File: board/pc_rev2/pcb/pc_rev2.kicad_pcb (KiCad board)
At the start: 4 copper layers, 200 x 100 mm, 104 parts, among them J1 GND Pins, J2 Conn_01x24, J3 Conn_01x24, J4 Conn_01x05, Q1 SSM3J332R, Q2 BSS138, Q3 BSS138, SW1 SW_Push, SW10 SW_Push, SW11 SW_Push, SW12 SW_Push, SW13 SW_Push, SW14 SW_Push, SW15 SW_Push, SW16 SW_Push, SW17 SW_Push, SW18 SW_Push, SW19 SW_Push, SW2 SW_Push, SW20 SW_Push, SW21 SW_Push, SW22 SW_Push, SW23 SW_Push, SW24 SW_Push, SW25 SW_Push, SW26 SW_Push, SW27 SW_Push, SW28 SW_Push, SW29 SW_Push, SW3 SW_Push, SW30 SW_Push, SW31 SW_Push, SW32 SW_Push, SW33 SW_Push, SW34 SW_Push, SW35 SW_Push, SW36 SW_Push, SW37 SW_Push, SW38 SW_Push, SW39 SW_Push, SW4 SW_Push, SW40 SW_Push, SW41 SW_Push, SW42 SW_Push, SW43 SW_Push, SW44 SW_Push, SW45 SW_Push, SW46 SW_Push, SW47 SW_Push, SW48 SW_Push, SW49 SW_Push, SW5 SW_Push, SW50 SW_Push, SW51 SW_Push, SW52 SW_Push, SW53 SW_Push, SW54 SW_Push, SW55 SW_Push, SW56 SW_Push, SW57 SW_Push, SW58 SW_Push, SW59 SW_Push, SW6 SW_Push, SW60 SW_Push, SW61 SW_Push, SW62 SW_Push, SW63 SW_Push, SW64 SW_Push, SW7 SW_Push, SW8 SW_Push, SW9 SW_Push, U1 AE-FT234X, U2 Tang_nano_9K, U3 SC2004CSWB-XA-LB-G, U4 NJM2742D, U5 4066, U6 TC75S103F, U7 NJU7109, U8 OLED

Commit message: 諸々改良＆基板デザイン（WIP）
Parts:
- removed H5: MountingHole, MountingHole:MountingHole_3.2mm_M3
- removed Q2, Q3: BSS138, Package_TO_SOT_SMD:SOT-23_Handsoldering
- removed SW1, SW10, SW11, SW12, SW13, SW14, SW15, SW16, SW17, SW18, SW19, SW2, SW20, SW21, SW22, SW23, SW24, SW25, SW26, SW27, SW28, SW29, SW3, SW30, SW31, SW32, SW33, SW34, SW35, SW36, SW37, SW38, SW39, SW4, SW40, SW41, SW42, SW43, SW44, SW45, SW46, SW47, SW48, SW49, SW5, SW50, SW51, SW52, SW53, SW54, SW55, SW56, SW57, SW58, SW59, SW6, SW60, SW61, SW62, SW63, SW64, SW7, SW8, SW9: SW_Push, Button_Switch_THT:SW_PUSH_6mm_H7.3mm
- removed U7: NJU7109, Package_TO_SOT_SMD:SOT-23-5
- added C1: 100nF, Capacitor_SMD:C_0603_1608Metric_Pad1.08x0.95mm_HandSolder, F.Cu at (109.6, 104.7)
- added C10: 100nF, Capacitor_SMD:C_0603_1608Metric_Pad1.08x0.95mm_HandSolder, F.Cu at (112.1, 50.5)
- added C11: 100pF, Capacitor_SMD:C_0603_1608Metric_Pad1.08x0.95mm_HandSolder, F.Cu at (113.4, 74.2)
- added C12: 100nF, Capacitor_SMD:C_0603_1608Metric_Pad1.08x0.95mm_HandSolder, F.Cu at (121.7, 67.2)
- added C13: 100nF, Capacitor_SMD:C_0603_1608Metric_Pad1.08x0.95mm_HandSolder, F.Cu at (117.9, 57.1)
- added C14: 100n, Capacitor_SMD:C_0603_1608Metric_Pad1.08x0.95mm_HandSolder, F.Cu at (66.4, 112.9)
- added C15: 100nF, Capacitor_SMD:C_0603_1608Metric_Pad1.08x0.95mm_HandSolder, F.Cu at (123.6, 53.2)
- added C16: 100nF, Capacitor_SMD:C_0603_1608Metric_Pad1.08x0.95mm_HandSolder, F.Cu at (132.5, 54.5)
- added C17: 100nF, Capacitor_SMD:C_0603_1608Metric_Pad1.08x0.95mm_HandSolder, F.Cu at (122.9, 125.6)
- added C9: 470uF, Capacitor_THT:CP_Radial_D8.0mm_P3.50mm, F.Cu at (129.0, 127.5)
- added D1: 1N4148, Diode_THT:D_DO-34_SOD68_P7.62mm_Horizontal, F.Cu at (64.5, 120.5)
- added D2: BAT54S, Package_TO_SOT_SMD:SOT-23, F.Cu at (132.5, 71.7)
- added J10: Conn_01x05, Connector_PinHeader_2.54mm:PinHeader_1x03_P2.54mm_Vertical, F.Cu at (123.6, 58.3)
- added J11: Conn_01x03, Connector_PinHeader_2.54mm:PinHeader_1x03_P2.54mm_Vertical, F.Cu at (140.7, 52.0)
- added J12: GND Pins, Connector_PinHeader_2.54mm:PinHeader_1x02_P2.54mm_Vertical, F.Cu at (100.1, 130.7)
- added J13: Conn_01x02, Connector_PinHeader_2.54mm:PinHeader_1x02_P2.54mm_Vertical, F.Cu at (131.2, 104.7)
- added J14: Conn_01x03, Connector_PinHeader_2.54mm:PinHeader_1x03_P2.54mm_Vertical, F.Cu at (140.7, 85.0)
- added J15: INPUT, Connector_JST:JST_XH_S3B-XH-A_1x03_P2.50mm_Horizontal, F.Cu at (51.8, 118.0)
- added J16: OUTPUT, Connector_JST:JST_XH_S3B-XH-A_1x03_P2.50mm_Horizontal, F.Cu at (51.8, 105.3)
- added J17: GND Pins, Connector_PinHeader_2.54mm:PinHeader_1x02_P2.54mm_Vertical, F.Cu at (138.2, 99.0)
- added J18: Conn_01x05, Connector_PinHeader_2.54mm:PinHeader_1x03_P2.54mm_Vertical, F.Cu at (100.1, 115.5)
- added J19: Conn_01x02, Connector_PinHeader_2.54mm:PinHeader_1x02_P2.54mm_Vertical, F.Cu at (131.2, 81.8)
- added J20: Conn_01x03, Connector_PinHeader_2.54mm:PinHeader_1x03_P2.54mm_Vertical, F.Cu at (124.8, 83.7)
- added J21: Conn_Grove_Host, uchan:Grove_1x04_P2mm_THT_Horizontal, F.Cu at (72.1, 128.8)
- added J5: Conn_Grove_Host, uchan:Grove_1x04_P2mm_THT_Horizontal, F.Cu at (107.7, 41.1)
- added J6: Conn_01x03, Connector_JST:JST_XH_S2B-XH-A_1x02_P2.50mm_Horizontal, F.Cu at (138.2, 107.8)
- added J7: Conn_01x03, Connector_JST:JST_XH_S2B-XH-A_1x02_P2.50mm_Horizontal, F.Cu at (138.2, 120.5)
- added J8: Conn_Grove-Analog_Host, uchan:Grove_1x04_P2mm_THT_Horizontal, F.Cu at (138.2, 62.1)
- added J9: Conn_Grove-Analog_Host, uchan:Grove_1x04_P2mm_THT_Horizontal, F.Cu at (138.2, 73.9)
- added R10: 100k, Resistor_SMD:R_0603_1608Metric_Pad0.98x0.95mm_HandSolder, F.Cu at (118.5, 86.9)
- added R11: 100k, Resistor_SMD:R_0603_1608Metric_Pad0.98x0.95mm_HandSolder, F.Cu at (114.0, 90.1)
- added R12: 33, Resistor_SMD:R_0603_1608Metric_Pad0.98x0.95mm_HandSolder, F.Cu at (117.9, 116.1)
- added R13: 33, Resistor_SMD:R_0603_1608Metric_Pad0.98x0.95mm_HandSolder, F.Cu at (115.3, 116.1)
- added R14: 10k, Resistor_SMD:R_0603_1608Metric_Pad0.98x0.95mm_HandSolder, F.Cu at (119.8, 121.8)
- added R15: 10k, Resistor_SMD:R_0603_1608Metric_Pad0.98x0.95mm_HandSolder, F.Cu at (133.7, 119.3)
- added R17: 22k, Resistor_SMD:R_0603_1608Metric_Pad0.98x0.95mm_HandSolder, F.Cu at (100.1, 62.8)
- added R18: 11k, Resistor_SMD:R_0603_1608Metric_Pad0.98x0.95mm_HandSolder, F.Cu at (105.2, 63.4)
- added R19: 22k, Resistor_SMD:R_0603_1608Metric_Pad0.98x0.95mm_HandSolder, F.Cu at (100.1, 67.2)
- added R20: 11k, Resistor_SMD:R_0603_1608Metric_Pad0.98x0.95mm_HandSolder, F.Cu at (105.2, 67.9)
- added R21: 22k, Resistor_SMD:R_0603_1608Metric_Pad0.98x0.95mm_HandSolder, F.Cu at (100.1, 71.7)
- added R22: 11k, Resistor_SMD:R_0603_1608Metric_Pad0.98x0.95mm_HandSolder, F.Cu at (105.2, 72.3)
- added R23: 22k, Resistor_SMD:R_0603_1608Metric_Pad0.98x0.95mm_HandSolder, F.Cu at (100.1, 76.1)
- added R24: 11k, Resistor_SMD:R_0603_1608Metric_Pad0.98x0.95mm_HandSolder, F.Cu at (105.2, 76.7)
- added R25: 22k, Resistor_SMD:R_0603_1608Metric_Pad0.98x0.95mm_HandSolder, F.Cu at (100.1, 79.9)
- added R26: 11k, Resistor_SMD:R_0603_1608Metric_Pad0.98x0.95mm_HandSolder, F.Cu at (105.2, 81.2)
- added R27: 22k, Resistor_SMD:R_0603_1608Metric_Pad0.98x0.95mm_HandSolder, F.Cu at (100.1, 84.4)
- added R28: 11k, Resistor_SMD:R_0603_1608Metric_Pad0.98x0.95mm_HandSolder, F.Cu at (105.2, 85.6)
- added R29: 22k, Resistor_SMD:R_0603_1608Metric_Pad0.98x0.95mm_HandSolder, F.Cu at (100.1, 88.8)
- added R30: 11k, Resistor_SMD:R_0603_1608Metric_Pad0.98x0.95mm_HandSolder, F.Cu at (105.2, 90.1)
- added R31: 22k, Resistor_SMD:R_0603_1608Metric_Pad0.98x0.95mm_HandSolder, F.Cu at (100.1, 93.3)
- added R32: 22k, Resistor_SMD:R_0603_1608Metric_Pad0.98x0.95mm_HandSolder, F.Cu at (105.2, 94.5)
- added R33: 390, uchan:R_Axial_CF25_CFS50_L6.3mm_D2.3mm_P7.62mm_Horizontal, F.Cu at (56.9, 118.0)
- added R34: 33, uchan:R_Axial_CF25_CFS50_L6.3mm_D2.3mm_P7.62mm_Horizontal, F.Cu at (64.5, 105.3)
- added R35: 10, uchan:R_Axial_CF25_CFS50_L6.3mm_D2.3mm_P7.62mm_Horizontal, F.Cu at (64.5, 107.8)
- added R36: 4.7k, Resistor_SMD:R_0603_1608Metric_Pad0.98x0.95mm_HandSolder, F.Cu at (69.0, 109.8)
- added R37: 100k, Resistor_SMD:R_0603_1608Metric_Pad0.98x0.95mm_HandSolder, F.Cu at (118.5, 93.3)
- added R38: 10k, Resistor_SMD:R_0603_1608Metric_Pad0.98x0.95mm_HandSolder, F.Cu at (128.7, 75.5)
- added U10: MCP1501-30xCH, Package_TO_SOT_SMD:SOT-23-6, F.Cu at (127.4, 53.2)
- added U9: TLP2361, Package_SO:SO-5-6_4.55x3.7mm_P1.27mm, F.Cu at (60.1, 112.9)
- C2: value 1.5nF -> 100nF; footprint Capacitor_THT:C_Disc_D4.3mm_W1.9mm_P5.00mm -> Capacitor_SMD:C_0603_1608Metric_Pad1.08x0.95mm_HandSolder
- C3: value 680pF -> 100nF; footprint Capacitor_THT:C_Disc_D4.3mm_W1.9mm_P5.00mm -> Capacitor_SMD:C_0603_1608Metric_Pad1.08x0.95mm_HandSolder
- C4: value 100pF -> 2000pF; footprint Capacitor_THT:C_Disc_D4.3mm_W1.9mm_P5.00mm -> Capacitor_SMD:C_0603_1608Metric_Pad1.08x0.95mm_HandSolder
- C5: value 100nF -> 10uF
- C6: value 100nF -> 1uF
- J1: value GND Pins -> Conn_02x13_Odd_Even; footprint Connector_PinHeader_2.54mm:PinHeader_1x04_P2.54mm_Vertical -> Connector_PinHeader_2.54mm:PinHeader_2x14_P2.54mm_Vertical
- J2: value Conn_01x24 -> Conn_02x08_Row_Letter_Last; footprint Connector_PinHeader_2.54mm:PinHeader_1x24_P2.54mm_Vertical -> Connector_PinHeader_2.54mm:PinHeader_2x08_P2.54mm_Vertical
- J3: value Conn_01x24 -> Conn_02x06_Row_Letter_Last; footprint Connector_PinHeader_2.54mm:PinHeader_1x24_P2.54mm_Vertical -> Connector_PinHeader_2.54mm:PinHeader_2x06_P2.54mm_Vertical
- J4: value Conn_01x05 -> Conn_02x10_Row_Letter_Last; footprint Connector_PinHeader_2.54mm:PinHeader_1x05_P2.54mm_Vertical -> Connector_PinHeader_2.54mm:PinHeader_2x10_P2.54mm_Vertical
- LS1: value PKM13EPYH4000-A0 -> 13mm
- Q1: value SSM3J332R -> BC817BPN; footprint Package_TO_SOT_SMD:SOT-23_Handsoldering -> Package_TO_SOT_SMD:SOT-457T
- R1: value 47 -> 0.5M; footprint Resistor_THT:R_Axial_DIN0207_L6.3mm_D2.5mm_P7.62mm_Horizontal -> OptoDevice:R_LDR_D6.4mm_P3.4mm_Vertical
- R2: value 0.5M -> 2.2k; footprint OptoDevice:R_LDR_D6.4mm_P3.4mm_Vertical -> Resistor_SMD:R_0603_1608Metric_Pad0.98x0.95mm_HandSolder
- R3: value 16k -> 100k
- R4, R5: value 4.7k -> 100k
- R6: value 16k -> 20k
- R7: value 2k -> 200
- R8: value 100 -> 2.2k
- R9: value 2k -> 100k
- RV1: footprint Potentiometer_THT:Potentiometer_Vishay_T73XX_Horizontal -> uchan:Potentiometer_Suntan_TSR-3386K_Vertical
- RV2: footprint uchan:Potentiometer_Suntan_TSR-065_Vertical -> uchan:Potentiometer_Suntan_TSR-3386K_Vertical
- RV3: value 5k -> 50k; footprint Potentiometer_THT:Potentiometer_Vishay_T73XX_Horizontal -> uchan:Potentiometer_Suntan_TSR-3386K_Vertical
- U1: value AE-FT234X -> Tang_nano_9K; footprint uchan:AE-FT234X -> uchan:DIP-48_Tang-Nano-9K
- U2: value Tang_nano_9K -> SKU2782; footprint uchan:DIP-48_Tang-Nano-9K -> uchan:SKU2782
- U3: value SC2004CSWB-XA-LB-G -> LMV324B; footprint uchan:SC2004C_float -> Package_SO:TSSOP-14_4.4x5mm_P0.65mm
- U4: value NJM2742D -> LMV324B; footprint Package_DIP:DIP-8_W7.62mm -> Package_SO:TSSOP-14_4.4x5mm_P0.65mm
- U5: value 4066 -> TC74HC4066AF; footprint Package_DIP:DIP-14_W7.62mm -> Package_SO:SO-14_5.3x10.2mm_P1.27mm
- U6: value TC75S103F -> TPCMP231; footprint Package_TO_SOT_SMD:TSOT-23-5 -> Package_TO_SOT_SMD:SOT-23-5
- U8: value OLED -> 74HC4051; footprint uchan:OLED_Display_I2C -> Package_SO:SOIC-16W_5.3x10.2mm_P1.27mm
- moved H2 210.2 mm to (50.0, 130.0)
- moved J2 192.1 mm to (49.3, 49.4), turned to 0 degrees
- moved J3 156.4 mm to (89.9, 39.3), turned to 0 degrees
- moved U2 141.7 mm to (100.1, 39.3), turned to 0 degrees
- moved J1 136.3 mm to (92.5, 90.1), turned to 180 degrees
- moved H4 134.5 mm to (140.0, 40.0)
- moved R4 116.2 mm to (112.1, 104.7), turned to 90 degrees
- moved R5 107.8 mm to (119.5, 100.9)
- moved U8 93.9 mm to (130.6, 62.1)
- moved H3 90.0 mm to (140.0, 130.0)
- moved RV3 85.2 mm to (126.6, 115.7)
- moved U1 80.7 mm to (82.3, 97.7), turned to 180 degrees
- moved U3 78.7 mm to (120.4, 107.2)
- moved RV1 73.5 mm to (84.8, 111.7), turned to -90 degrees
- moved Q1 73.0 mm to (122.9, 128.8), turned to 0 degrees
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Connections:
- C2 pad 1: Net-(C2-Pad1) -> /audio/mic_in
- C2 pad 2: /ADC/dac_out -> /audio/mic_opin
- C3 pad 2: Net-(U4B-+) -> +5V
- C4 pad 1: Net-(C4-Pad1) -> Net-(U3D--)
- C4 pad 2: GND -> /audio/mic_mid
- C5 pad 1: +5V -> Net-(C5-Pad1)
- C6 pad 1: GND -> Net-(C6-Pad1)
- C6 pad 2: +5V -> GND
- C7 pad 1: +5V -> Net-(C7-Pad1)
- C8 pad 1: +5V -> Net-(C8-Pad1)
- C8 pad 2: GND -> /audio/spk_opin
- J1 pad 2: GND -> /ADC/vref_d0
- J1 pad 4: GND -> /ADC/vref_d1
- J2 pad 1: Net-(J2-Pin_1) -> GND
- J2 pad 10: /ROW6 -> /mcu/gpio4
- J2 pad 11: /ROW7 -> GND
- J2 pad 12: /ROW8 -> /mcu/gpio5
- J2 pad 13: /SCL -> GND
- J2 pad 14: /SDA -> /beep
- J2 pad 15: Net-(J2-Pin_15) -> GND
- J2 pad 16: Net-(J2-Pin_16) -> /mcu/gpio7
- J2 pad 2: Net-(J2-Pin_2) -> /mcu/gpio0
- J2 pad 3: Net-(J2-Pin_3) -> GND
- J2 pad 4: Net-(J2-Pin_4) -> /mcu/gpio1
- J2 pad 5: /ROW1 -> GND
- J2 pad 6: /ROW2 -> /mcu/gpio2
- J2 pad 7: /ROW3 -> GND
- J2 pad 8: /ROW4 -> /mcu/gpio3
- J2 pad 9: /ROW5 -> GND
- J3 pad 1: /RS -> /uart_rx
- J3 pad 10: /RW -> GND
- J3 pad 11: /E -> /sericon_tx
- J3 pad 12: Net-(J3-Pin_12) -> GND
- J3 pad 2: /COL8 -> GND
- J3 pad 3: /COL7 -> /uart_tx
- J3 pad 4: /COL6 -> GND
- J3 pad 5: /COL5 -> /msmp_rx
- J3 pad 6: /COL4 -> GND
- J3 pad 7: /COL3 -> /msmp_tx
- J3 pad 8: /COL2 -> GND
- J3 pad 9: /COL1 -> /sericon_rx
- J4 pad 1: /ADC/sh_buf -> GND
- J4 pad 2: /ADC/ain_buf -> /mcu/dbgio0
- J4 pad 3: /ADC/sh_on_5v -> GND
- J4 pad 4: /ADC/dac_out -> /mcu/dbgio1
- Q1 pad 1: Net-(J3-Pin_12) -> /audio/spk_opout
- Q1 pad 2: +5V -> Net-(Q1A-B1)
- Q1 pad 3: Net-(Q1-D) -> GND
- R1 pad 1: Net-(Q1-D) -> +3.3V
- R1 pad 2: Net-(U3-A) -> /ADC/ain1
- R2 pad 1: +5V -> +3.3V
- R2 pad 2: /ADC/ain -> /audio/mic_in
- R3 pad 1: /adc_dac_pwm -> +3.3V
- R3 pad 2: Net-(C2-Pad1) -> Net-(U3A-+)
- R4 pad 1: /SCL -> Net-(U3A-+)
- R4 pad 2: +3.3V -> GND
- R5 pad 1: /SDA -> /audio/mic_opin
- R5 pad 2: +3.3V -> GNDREF
- R6 pad 1: Net-(C2-Pad1) -> Net-(U3D--)
- R6 pad 2: Net-(U4B-+) -> /audio/mic_mid
- R7 pad 1: +5V -> Net-(U3D--)
- R7 pad 2: /ADC/sh_on_5v -> Net-(C5-Pad1)
- R8 pad 1: Net-(U6-+) -> Net-(U3C--)
- R8 pad 2: Net-(C4-Pad1) -> Net-(C6-Pad1)
- R9 pad 1: +3.3V -> +5V
- R9 pad 2: /adc_cmp -> Net-(C7-Pad1)
- RV1 pad 1: +3.3V -> /beep
- RV1 pad 2: Net-(U3-VO) -> Net-(LS1-Pad1)
- RV2 pad 1: /ADC/ain -> /ADC/ain1
- RV3 pad 1: Net-(J3-Pin_13) -> Net-(U3C--)
- RV3 pad 2: Net-(LS1-Pad1) -> Net-(U3C--)
- RV3 pad 3: GND -> Net-(R38-Pad1)
- U1 pad 1: unconnected-(U1-5V-Pad1) -> /mcu/tf_cs
- U1 pad 2: GND -> /mcu/tf_mosi
- U1 pad 3: /RX -> /mcu/tf_sclk
- U1 pad 4: /TX -> /mcu/tf_miso
- U1 pad 5: unconnected-(U1-CB0-Pad5) -> /ADC/vref_d0
- U2 pad 1: Net-(J2-Pin_1) -> unconnected-(U2-DTR-Pad1)
- U2 pad 2: Net-(J2-Pin_2) -> /uart_tx
- U2 pad 3: Net-(J2-Pin_3) -> /uart_rx
- U2 pad 4: Net-(J2-Pin_4) -> unconnected-(U2-VCC-Pad4)
- U2 pad 5: /ROW1 -> unconnected-(U2-CTS-Pad5)
- U2 pad 6: /ROW2 -> GND
- U3 pad 1: GND -> GNDREF
- U3 pad 10: unconnected-(U3-DB3-Pad10) -> /audio/mic_mid
- U3 pad 11: /DB4 -> GND
- U3 pad 12: /DB5 -> /audio/mic_opin
- U3 pad 13: /DB6 -> Net-(U3D--)
- U3 pad 14: /DB7 -> /audio/mic_mid
- U3 pad 2: +3.3V -> GNDREF
- U3 pad 3: Net-(U3-VO) -> Net-(U3A-+)
- U3 pad 4: /RS -> +5V
- U3 pad 5: /RW -> /audio/spk_opin
- U3 pad 6: /E -> Net-(U3B--)
- U3 pad 7: unconnected-(U3-DB0-Pad7) -> /audio/spk_mid
- U3 pad 8: unconnected-(U3-DB1-Pad8) -> Net-(R38-Pad1)
- U3 pad 9: unconnected-(U3-DB2-Pad9) -> Net-(U3C--)
- U4 pad 1: /ADC/ain_buf -> /ADC/sh_buf
- U4 pad 2: /ADC/ain_buf -> /ADC/sh_buf
- U4 pad 3: /ADC/ain -> Net-(U4A-+)
- U4 pad 4: GND -> +5V
- U4 pad 5: Net-(U4B-+) -> GND
- U4 pad 6: /ADC/dac_out -> Net-(U4B--)
- U4 pad 7: /ADC/dac_out -> Net-(U4B--)
- U4 pad 8: +5V -> /ADC/ain_buf
- U5 pad 1: /ADC/ain_buf -> /ADC/dac_out
- U5 pad 10: unconnected-(U5-Pad10) -> GND
- U5 pad 11: unconnected-(U5-Pad11) -> GND
- U5 pad 13: /ADC/sh_on_5v -> /audio/spk_on
- U5 pad 14: +5V -> +3.3V
- U5 pad 2: Net-(U6-+) -> Net-(C8-Pad1)
- U5 pad 3: unconnected-(U5-Pad3) -> /ADC/ain_buf
- U5 pad 4: unconnected-(U5-Pad4) -> Net-(U4A-+)
- U5 pad 5: GND -> /ADC/sh_on
- U5 pad 8: unconnected-(U5-Pad8) -> GND
- U5 pad 9: unconnected-(U5-Pad9) -> GND
- U6 pad 1: /ADC/sh_buf -> /ADC/cmp
- U6 pad 3: Net-(U6-+) -> /ADC/sh_buf
- U6 pad 4: /ADC/sh_buf -> /ADC/dac_raw
- U6 pad 5: +5V -> +3.3V
- U8 pad 1: GND -> /ADC/ain4
- U8 pad 2: +3.3V -> /ADC/dac_out
- U8 pad 3: /SCL -> Net-(U4C-+)
- U8 pad 4: /SDA -> Net-(U10-OUT)
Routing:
- net /COL6: track 330.2 -> 0.00 mm, vias 2 -> 0
- net /COL1: track 294.0 -> 0.00 mm, vias 2 -> 0
- net /COL7: track 293.3 -> 0.00 mm, vias 1 -> 0
- net /COL2: track 293.2 -> 0.00 mm, vias 2 -> 0
- net /COL3: track 275.4 -> 0.00 mm, vias 2 -> 0
- net /COL4: track 274.7 -> 0.00 mm, vias 2 -> 0
- net /COL5: track 267.7 -> 0.00 mm, vias 2 -> 0
- net /ROW6: track 266.0 -> 0.00 mm, vias 1 -> 0
- net /ROW7: track 240.1 -> 0.00 mm, vias 1 -> 0
- net /ROW2: track 236.8 -> 0.00 mm, vias 2 -> 0
- net /COL8: track 229.6 -> 0.00 mm
- net /ROW1: track 226.0 -> 0.00 mm, vias 1 -> 0
- net /ROW5: track 218.9 -> 0.00 mm, vias 1 -> 0
- net /ROW3: track 215.7 -> 0.00 mm, vias 1 -> 0
- net /RS: track 199.8 -> 0.00 mm
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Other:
- board size 200 x 100 mm -> 100 x 100 mm
- copper layers 4 -> 2
- board text added: "1.65V"
- board text added: "10k"
- board text added: "2.5V"
- board text added: "33"
- board text added: "470uF"
- board text added: "50k"
- board text removed: ", <"
- board text removed: "- ="
- board text removed: ". >"
- board text removed: "/ ?"
- board text removed: "0"
- board text removed: "1 !"
- board text removed: "2 {dblquote}"
- board text removed: "2024/09/27 Rev.1 Kota Uchida Cybozu Labs, Inc."
- board text removed: "3 #"
- board text removed: "3.3V"
- board text removed: "4 $"
- board text removed: "5 %"
- board text removed: "5V"
- board text removed: "6 &"
- board text removed: "7 '"
- board text removed: "8 ("
- board text removed: "9 )"
- board text removed: ": *"
- board text removed: "; +"
- board text removed: "@ `"
- board text removed: "A"
- board text removed: "Alt"
- board text removed: "B"
- board text removed: "BL"
- board text removed: "BS"
- board text removed: "C"
- board text removed: "COL1"
- board text removed: "COL2"
- board text removed: "COL5"
- board text removed: "COL6"
- board text removed: "COL7"
- board text removed: "COL8"
- board text removed: "CS"
- board text removed: "Caps"
- board text removed: "ComProc PC"
- board text removed: "Contrast"
- board text removed: "Ctrl"
- board text removed: "D"
- board text removed: "DB4"
- board text removed: "DB5"
- board text removed: "DB6"
- board text removed: "DB7"
- board text removed: "E"
- board text removed: "E/J"
- board text removed: "Enter"
- board text removed: "F"
- board text removed: "G"
- board text removed: "GND"
- board text removed: "H"
- board text removed: "I"
- board text removed: "J"
- board text removed: "JLCJLCJLCJLC"
- board text removed: "K"
- board text removed: "Kana"
- board text removed: "L"
- board text removed: "M"
- board text removed: "MO"
- board text removed: "N"
- board text removed: "O"
- board text removed: "P"
- board text removed: "P41"
- board text removed: "P42"
- board text removed: "P51"
- board text removed: "P68"
- board text removed: "P69"
- board text removed: "P70"
- board text removed: "P71"
- board text removed: "P72"
- board text removed: "P73"
- board text removed: "P74"
- board text removed: "Q"
- board text removed: "R"
- board text removed: "ROW1"
- board text removed: "ROW2"
- board text removed: "ROW3"
- board text removed: "ROW4"
- board text removed: "ROW5"
- board text removed: "ROW6"
- board text removed: "ROW7"
- board text removed: "ROW8"
- board text removed: "RS"
- board text removed: "RW"
- board text removed: "RX"
- board text removed: "S"
- board text removed: "SCL"
- board text removed: "SDA"
- board text removed: "Shift"
- board text removed: "Space"
- board text removed: "T"
- board text removed: "TF_MISO"
- board text removed: "TF_SCLK"
- board text removed: "TX"
- board text removed: "Tab"
- board text removed: "U"
- board text removed: "V"
- board text removed: "Volume"
- board text removed: "W"
- board text removed: "X"
- board text removed: "Y"
- board text removed: "Z"
- board text removed: "[ {"
- board text removed: "\ _"
- board text removed: "] }"
- board text removed: "^ ~"
- board text removed: "ain"
- board text removed: "cmp"
- board text removed: "dac"
- board text removed: "dac_pwm"
- board text removed: "sh"
- board text removed: "sh_ctl"
- board text removed: "shon"
- board text removed: "←"
- board text removed: "↑"
- board text removed: "→"
- board text removed: "↓"
- board text removed: "変換"
- board text removed: "無変換"
- board text removed: "￥ |"

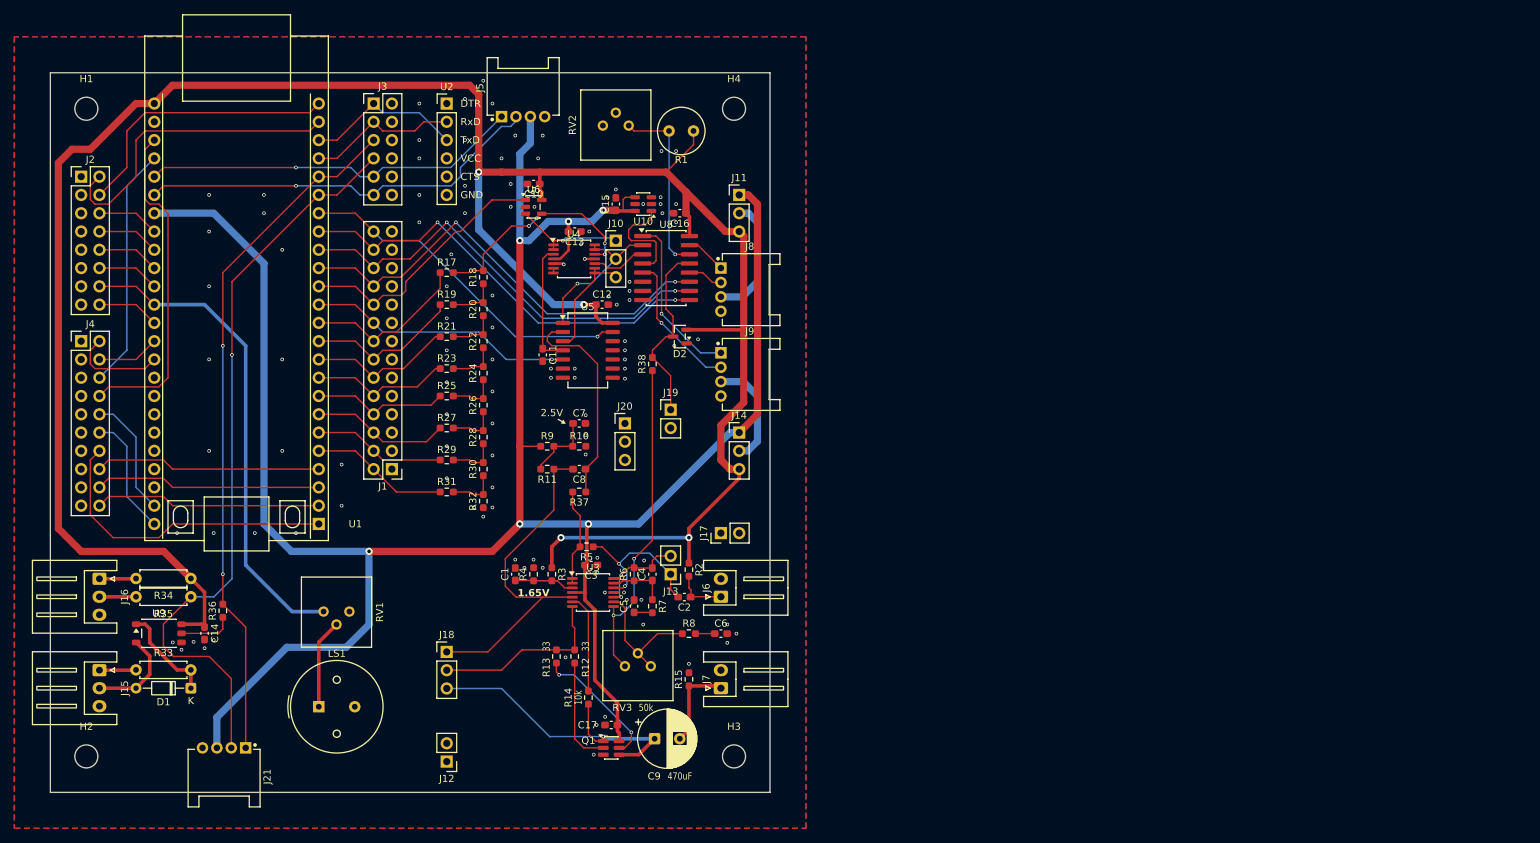
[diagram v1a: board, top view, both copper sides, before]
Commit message: Rev.2基板のシルク印刷を整える
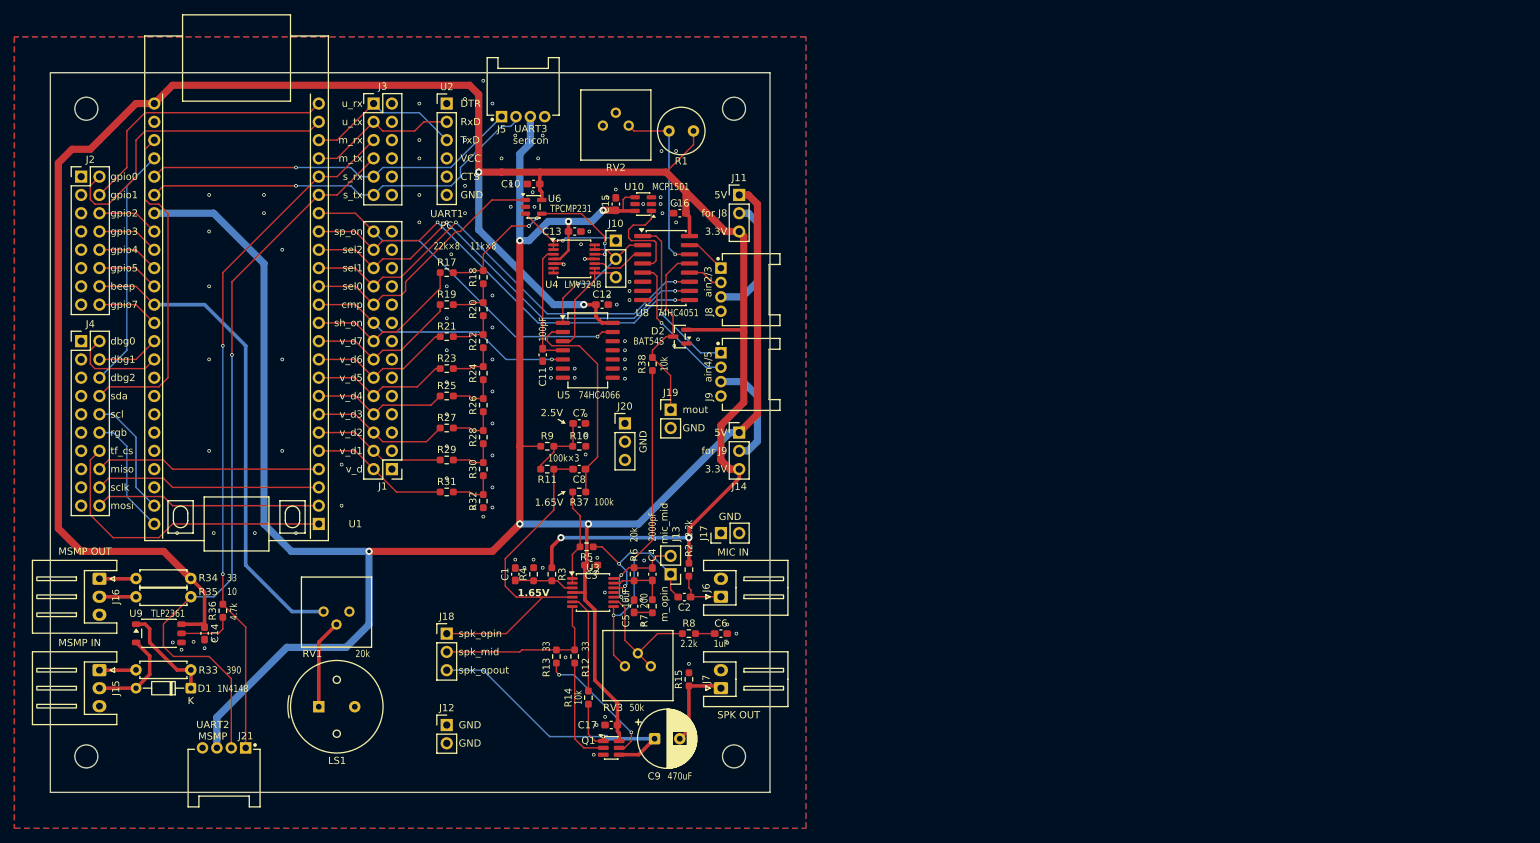
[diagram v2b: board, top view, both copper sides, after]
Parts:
- moved J12 5.08 mm to (100.1, 125.6), turned to 0 degrees
- moved J18 2.54 mm to (100.1, 112.9)
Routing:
- net /audio/spk_opout: track 44.9 -> 45.9 mm
- net /audio/spk_opin: track 48.2 -> 47.1 mm
- net /audio/spk_mid: track 25.1 -> 24.1 mm
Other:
- board text added: "10"
- board text added: "100k"
- board text added: "100k×3"
- board text added: "100pF"
- board text added: "10uF"
- board text added: "11k×8"
- board text added: "1N4148"
- board text added: "1uF"
- board text added: "2.2k"
- board text added: "200"
- board text added: "2000pF"
- board text added: "20k"
- board text added: "22k×8"
- board text added: "3.3V"
- board text added: "390"
- board text added: "4.7k"
- board text added: "5V"
- board text added: "74HC4051"
- board text added: "74HC4066"
- board text added: "BAT54S"
- board text added: "GND"
- board text added: "LMV324B"
- board text added: "MCP1501"
- board text added: "MIC IN"
- board text added: "MSMP IN"
- board text added: "MSMP OUT"
- board text added: "SPK OUT"
- board text added: "TLP2361"
- board text added: "TPCMP231"
- board text added: "UART1 PC"
- board text added: "UART2 MSMP"
- board text added: "UART3 sericon"
- board text added: "ain2/3"
- board text added: "ain4/5"
- board text added: "beep"
- board text added: "cmp"
- board text added: "dbg0"
- board text added: "dbg1"
- board text added: "dbg2"
- board text added: "for J8"
- board text added: "for J9"
- board text added: "gpio0"
- board text added: "gpio1"
- board text added: "gpio2"
- board text added: "gpio3"
- board text added: "gpio4"
- board text added: "gpio5"
- board text added: "gpio7"
- board text added: "m_opin"
- board text added: "m_rx"
- board text added: "m_tx"
- board text added: "mic_mid"
- board text added: "miso"
- board text added: "mosi"
- board text added: "mout"
- board text added: "rgb"
- board text added: "s_rx"
- board text added: "s_tx"
- board text added: "scl"
- board text added: "sclk"
- board text added: "sda"
- board text added: "sel0"
- board text added: "sel1"
- board text added: "sel2"
- board text added: "sh_on"
- board text added: "sp_on"
- board text added: "spk_mid"
- board text added: "spk_opin"
- board text added: "spk_opout"
- board text added: "tf_cs"
- board text added: "u_rx"
- board text added: "u_tx"
- board text added: "v_d"
- board text added: "v_d1"
- board text added: "v_d2"
- board text added: "v_d3"
- board text added: "v_d4"
- board text added: "v_d5"
- board text added: "v_d6"
- board text added: "v_d7"

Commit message: ポップノイズ防止用コンデンサ追加＆シルク微修正
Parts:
- added C18: 10nF, Capacitor_SMD:C_0603_1608Metric_Pad1.08x0.95mm_HandSolder, F.Cu at (122.9, 93.2)
- moved J18 2.54 mm to (100.1, 115.5)
- moved LS1 2.54 mm to (79.8, 123.1)
- moved RV1 2.46 mm to (82.3, 111.7)
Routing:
- net +5V: track 327.5 -> 324.4 mm
- net Net-(C18-Pad1): track 29.9 -> 32.5 mm
- net /beep: track 67.7 -> 65.3 mm
- net /audio/spk_opout: track 45.9 -> 44.9 mm
- net /audio/spk_opin: track 47.1 -> 48.2 mm
- net /audio/spk_mid: track 24.1 -> 25.1 mm
- net GND: vias 111 -> 114
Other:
- board text added: "01"
- board text added: "100k×2"
- board text added: "10nF"
- board text added: "2026/08/26 Rev.2 Kota Uchida Cybozu Labs, Inc."
- board text added: "8bit R-2R DAC"
- board text added: "BuntanPC"
- board text added: "CMP"
- board text added: "Hold Value"
- board text added: "Input"
- board text added: "Ref Vol"
- board text added: "SIG"
- board text added: "Sample & Hold"
- board text added: "Select"
- board text added: "mic_out"
- board text added: "opin"
- board text removed: "m_opin"
- board text removed: "mout"

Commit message: I2C用Groveコネクタを追加
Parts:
- added J22: Conn_Grove_I2C, uchan:Grove_1x04_P2mm_THT_Horizontal, F.Cu at (84.2, 128.8)
- added J23: Conn_01x03, Connector_PinHeader_2.54mm:PinHeader_1x03_P2.54mm_Vertical, F.Cu at (89.9, 125.6)
- moved LS1 15.3 mm to (78.6, 107.9)
- moved RV1 10.2 mm to (81.0, 121.8)
- moved J8 0.63 mm to (138.8, 62.1)
- moved J9 0.63 mm to (138.8, 73.9)
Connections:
- net /mcu/sda renamed /sda
- J4 pad 10: /mcu/scl -> /scl
- R1 pad 2: /ADC/ain1 -> /ADC/ain0
- RV2 pad 1: /ADC/ain1 -> /ADC/ain0
- U1 pad 47: /mcu/scl -> /mcu/rgbled
- U1 pad 48: /mcu/rgbled -> /scl
- U8 pad 13: /audio/mic_out -> /ADC/ain0
- U8 pad 14: /ADC/ain1 -> /audio/mic_out
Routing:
- net /scl: track 0.00 -> 66.9 mm
- net /sda: track 46.2 -> 105.5 mm, vias 0 -> 2
- net +3.3V: track 330.0 -> 386.6 mm
- net /ADC/ain0: track 0.00 -> 26.7 mm, vias 0 -> 1
- net /ADC/ain1: track 25.4 -> 0.00 mm, vias 1 -> 0
- net /mcu/scl: track 17.0 -> 0.00 mm
- net +5V: track 324.4 -> 338.0 mm
- net Net-(J22-VCC): track 0.00 -> 13.1 mm
- net /beep: track 65.3 -> 73.8 mm, vias 0 -> 1
- net Net-(LS1-Pad1): track 12.5 -> 15.0 mm
- net /mcu/tf_cs: track 43.3 -> 41.3 mm
- net /audio/mic_out: track 25.8 -> 27.3 mm
- net /mcu/rgbled: track 17.0 -> 15.5 mm
- net Net-(J14-Pin_2): track 15.3 -> 14.6 mm
- net Net-(J11-Pin_2): track 17.3 -> 16.6 mm
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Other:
- board text added: "10u"
- board text added: "2026/08/27 Rev.2 Kota Uchida Cybozu Labs, Inc."
- board text added: "BC817"
- board text added: "J22"
- board text added: "SCL"
- board text added: "SDA"
- board text added: "VCC"
- board text removed: "10uF"
- board text removed: "2026/08/26 Rev.2 Kota Uchida Cybozu Labs, Inc."

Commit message: オペアンプ入力保護抵抗を追加
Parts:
- added R16: 10k, Resistor_SMD:R_0603_1608Metric_Pad0.98x0.95mm_HandSolder, F.Cu at (113.4, 107.9)
- moved R12 2.54 mm to (115.3, 116.1)
- moved R13 2.54 mm to (117.9, 116.1)
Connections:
- U3 pad 5: /audio/spk_opin -> Net-(U3B-+)
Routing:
- net /audio/spk_opin: track 48.2 -> 41.1 mm
- net Net-(U3B-+): track 0.00 -> 3.22 mm
- net Net-(Q1B-B2): track 18.4 -> 16.2 mm
- net Net-(Q1A-B1): track 15.0 -> 16.1 mm
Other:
- board text added: "spk"
- board text added: "v_d0"
- board text removed: "sp_on"
- board text removed: "v_d"
